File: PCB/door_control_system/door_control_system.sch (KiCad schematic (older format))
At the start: 48 parts, among them K1 DIPxx-1Axx-13x, Q1 2N7000, Q10 BSS84, Q11 BSS84, Q12 BSS84, Q13 BSS84, Q14 2N7000, Q15 2N7000, Q16 2N7000, Q17 2N7000, Q2 2N7000, Q3 2N7000, Q4 2N7000, Q5 2N7000, Q6 2N7000, Q7 2N7000, Q8 2N7000, Q9 2N7000, SW1 SW_MEC_5G, SW10 SW_MEC_5G, SW11 SW_MEC_5G, SW12 SW_MEC_5G, SW2 SW_MEC_5G, SW3 SW_MEC_5G, SW4 SW_MEC_5G, SW5 SW_MEC_5G, SW6 SW_MEC_5G, SW7 SW_MEC_5G, SW8 SW_MEC_5G, SW9 SW_MEC_5G, U1 HDSP-A401, U2 HDSP-A401, U3 HDSP-A401, U4 HDSP-A401

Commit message: Update schematic add lock controller and lock controller tb
- Schematic
- Lock controller + TB
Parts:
- added C1: 100u, symbol Device:CP
- added C2: 4u7, symbol Device:CP
- added FB1: Ferrite_Bead, symbol Device:Ferrite_Bead
- added J1, J2, J3: Conn_02x06_Top_Bottom, symbol Connector_Generic:Conn_02x06_Top_Bottom
- added J4: Barrel_Jack, symbol Connector:Barrel_Jack
- added J5: Screw_Terminal_01x02, symbol Connector:Screw_Terminal_01x02
- added R14, R15, R16, R18, R19, R20, R21, R22, R23, R24, R25, R26, R27, R28, R29, R30: 10k, symbol Device:R
- added R17: 100R, symbol Device:R
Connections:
- net labels added: FPGA_DO, VCC
- net labels removed: +5V, DOOR_SOLENOID, FPGA_DOOR_OPEN
- wire segments 225 -> 340
- no-connect marks 0 -> 4
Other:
- moved on the sheet: D1, K1, Q7, R1

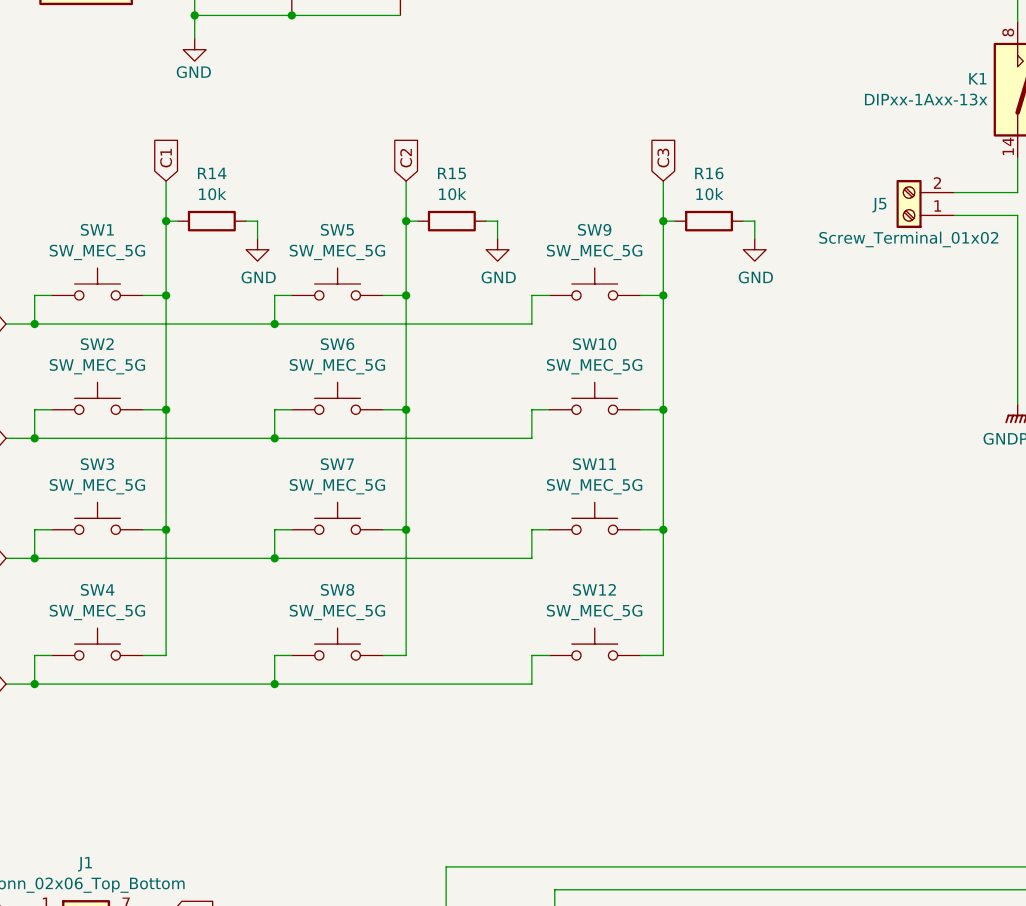
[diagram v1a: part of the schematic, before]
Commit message: Add waveform and fix schematic
Add waveform and fix schematic
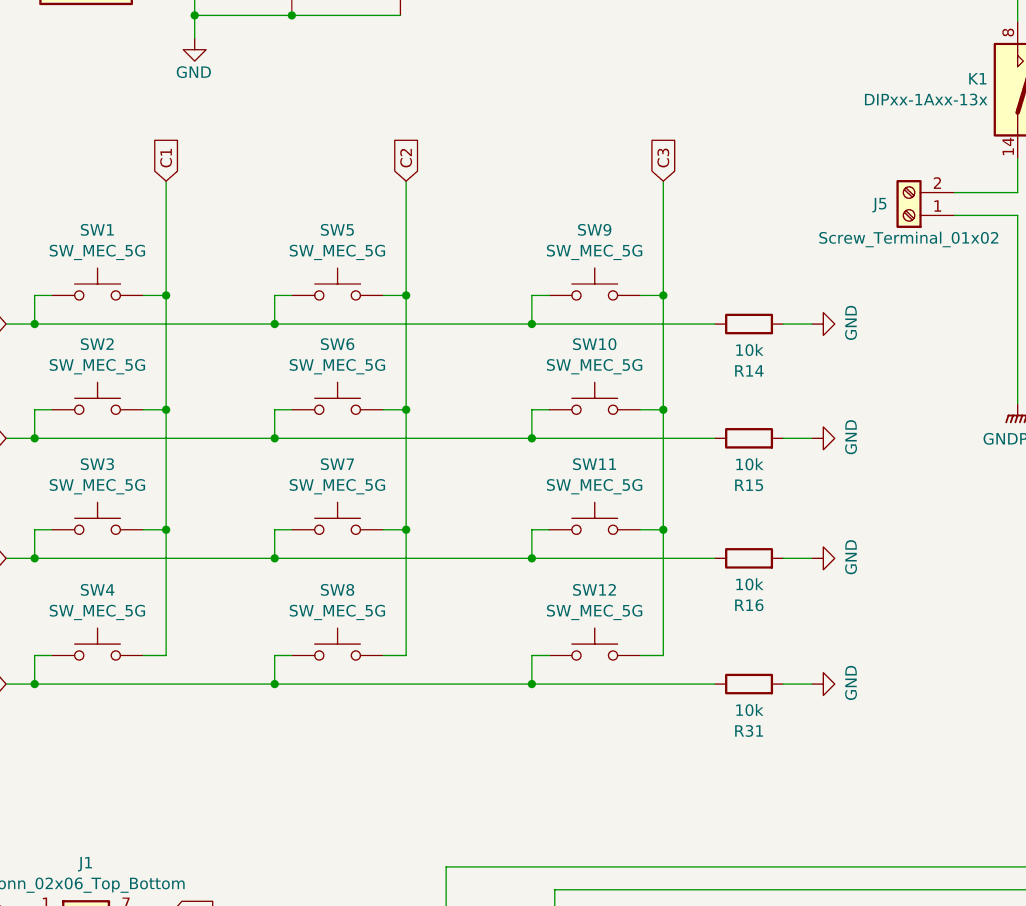
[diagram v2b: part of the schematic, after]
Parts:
- added R31: 10k, symbol Device:R
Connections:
- net C1: no longer R14.2
- net C2: no longer R15.2
- net C3: no longer R16.2
- net GND: now also R14.2, R15.2, R16.2, R31.2; no longer R14.1, R15.1, R16.1
- net R1: now also R14.1
- net R2: now also R15.1
- net R3: now also R16.1
- net R4: now also R31.1
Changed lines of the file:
@@
 	3875 2425 3975 2425
 Wire Wire Line
-	3975 2425 3975 2100
-Wire Wire Line
 	2750 2425 2850 2425
-Wire Wire Line
-	2850 2425 2850 2100
 Wire Wire Line
 	1700 2425 1800 2425
@@
 Text GLabel 3975 1925 1    50   Input ~ 0
 C3
-Text GLabel 1100 2550 0    50   Input ~ 0
-R1
-Text GLabel 1100 3050 0    50   Input ~ 0
-R2
-Text GLabel 1100 3575 0    50   Input ~ 0
-R3
-Text GLabel 1100 4125 0    50   Input ~ 0
-R4
 Wire Wire Line
 	1300 2925 1225 2925
@@
 Wire Wire Line
 	1225 4125 1100 4125
-$Comp
-L Device:R R14
-U 1 1 60801366
-P 2000 2100
-F 0 "R14" V 1793 2100 50  0000 C CNN
-F 1 "10k" V 1884 2100 50  0000 C CNN
-F 2 "" V 1930 2100 50  0001 C CNN
-F 3 "~" H 2000 2100 50  0001 C CNN
-	1    2000 2100
-	0    1    1    0
-$EndComp
-$Comp
-L my_power:GND #PWR017
-U 1 1 60832058
-P 2200 2175
-F 0 "#PWR017" H 2200 1925 50  0001 C CNN
-F 1 "GND" H 2205 2002 50  0000 C CNN
-F 2 "" H 2200 2175 50  0001 C CNN
-F 3 "" H 2200 2175 50  0001 C CNN
-	1    2200 2175
-	1    0    0    -1
-$EndComp
-Wire Wire Line
-	1800 1925 1800 2100
-Wire Wire Line
-	2200 2175 2200 2100
-Wire Wire Line
-	2200 2100 2150 2100
-Wire Wire Line
-	1850 2100 1800 2100
-Connection ~ 1800 2100
-Wire Wire Line
-	1800 2100 1800 2425
-$Comp
-L Device:R R15
-U 1 1 608D839D
-P 3050 2100
-F 0 "R15" V 2843 2100 50  0000 C CNN
-F 1 "10k" V 2934 2100 50  0000 C CNN
-F 2 "" V 2980 2100 50  0001 C CNN
-F 3 "~" H 3050 2100 50  0001 C CNN
-	1    3050 2100
-	0    1    1    0
-$EndComp
-$Comp
-L my_power:GND #PWR018
-U 1 1 608D83A3
-P 3250 2175
-F 0 "#PWR018" H 3250 1925 50  0001 C CNN
-F 1 "GND" H 3255 2002 50  0000 C CNN
-F 2 "" H 3250 2175 50  0001 C CNN
-F 3 "" H 3250 2175 50  0001 C CNN
-	1    3250 2175
-	1    0    0    -1
-$EndComp
-Wire Wire Line
-	3250 2175 3250 2100
-Wire Wire Line
-	3250 2100 3200 2100
-Wire Wire Line
-	2900 2100 2850 2100
-Connection ~ 2850 2100
-Wire Wire Line
-	2850 2100 2850 1925
-$Comp
-L Device:R R16
-U 1 1 608EA9CD
-P 4175 2100
-F 0 "R16" V 3968 2100 50  0000 C CNN
-F 1 "10k" V 4059 2100 50  0000 C CNN
-F 2 "" V 4105 2100 50  0001 C CNN
-F 3 "~" H 4175 2100 50  0001 C CNN
-	1    4175 2100
-	0    1    1    0
-$EndComp
-$Comp
-L my_power:GND #PWR019
-U 1 1 608EA9D3
-P 4375 2175
-F 0 "#PWR019" H 4375 1925 50  0001 C CNN
-F 1 "GND" H 4380 2002 50  0000 C CNN
-F 2 "" H 4375 2175 50  0001 C CNN
-F 3 "" H 4375 2175 50  0001 C CNN
-	1    4375 2175
-	1    0    0    -1
-$EndComp
-Wire Wire Line
-	4375 2175 4375 2100
-Wire Wire Line
-	4375 2100 4325 2100
-Wire Wire Line
-	4025 2100 3975 2100
-Connection ~ 3975 2100
-Wire Wire Line
-	3975 2100 3975 1925
 Wire Wire Line
 	6075 5525 6075 6300
@@
 Wire Wire Line
 	5525 1825 5525 1975
+Wire Wire Line
+	1800 1925 1800 2425
+Wire Wire Line
+	2850 1925 2850 2425
+Wire Wire Line
+	3975 1925 3975 2425
+$Comp
+L my_power:GND #PWR035
+U 1 1 608A0FBA
+P 4625 4125
+F 0 "#PWR035" H 4625 3875 50  0001 C CNN
+F 1 "GND" H 4630 3952 50  0000 C CNN
+F 2 "" H 4625 4125 50  0001 C CNN
+F 3 "" H 4625 4125 50  0001 C CNN
+	1    4625 4125
+	0    -1   -1   0
+$EndComp
+Wire Wire Line
+	4500 4125 4625 4125
+$Comp
+L Device:R R31
+U 1 1 608A0FB4
+P 4350 4125
+F 0 "R31" V 4143 4125 50  0000 C CNN
+F 1 "10k" V 4234 4125 50  0000 C CNN
+F 2 "" V 4280 4125 50  0001 C CNN
+F 3 "~" H 4350 4125 50  0001 C CNN
+	1    4350 4125
+	0    -1   -1   0
+$EndComp
+Text GLabel 1100 2550 0    50   Input ~ 0
+R1
+Text GLabel 1100 3050 0    50   Input ~ 0
+R2
+Text GLabel 1100 3575 0    50   Input ~ 0
+R3
+Text GLabel 1100 4125 0    50   Input ~ 0
+R4
+Wire Wire Line
+	4200 4125 3400 4125
+Connection ~ 3400 4125
+$Comp
+L my_power:GND #PWR019
+U 1 1 609B5E92
+P 4625 3575
+F 0 "#PWR019" H 4625 3325 50  0001 C CNN
+F 1 "GND" H 4630 3402 50  0000 C CNN
+F 2 "" H 4625 3575 50  0001 C CNN
+F 3 "" H 4625 3575 50  0001 C CNN
+	1    4625 3575
+	0    -1   -1   0
+$EndComp
+Wire Wire Line
+	4500 3575 4625 3575
+$Comp
+L Device:R R16
+U 1 1 609B5E99
+P 4350 3575
+F 0 "R16" V 4143 3575 50  0000 C CNN
+F 1 "10k" V 4234 3575 50  0000 C CNN
+F 2 "" V 4280 3575 50  0001 C CNN
+F 3 "~" H 4350 3575 50  0001 C CNN
+	1    4350 3575
+	0    -1   -1   0
+$EndComp
+Wire Wire Line
+	4200 3575 3400 3575
+Connection ~ 3400 3575
+$Comp
+L my_power:GND #PWR018
+U 1 1 60A22D19
+P 4625 3050
+F 0 "#PWR018" H 4625 2800 50  0001 C CNN
+F 1 "GND" H 4630 2877 50  0000 C CNN
+F 2 "" H 4625 3050 50  0001 C CNN
+F 3 "" H 4625 3050 50  0001 C CNN
+	1    4625 3050
+	0    -1   -1   0
+$EndComp
+Wire Wire Line
+	4500 3050 4625 3050
+$Comp
+L Device:R R15
+U 1 1 60A22D20
+P 4350 3050
+F 0 "R15" V 4143 3050 50  0000 C CNN
+F 1 "10k" V 4234 3050 50  0000 C CNN
+F 2 "" V 4280 3050 50  0001 C CNN
+F 3 "~" H 4350 3050 50  0001 C CNN
+	1    4350 3050
+	0    -1   -1   0
+$EndComp
+Wire Wire Line
+	4200 3050 3400 3050
+Connection ~ 3400 3050
+$Comp
+L my_power:GND #PWR017
+U 1 1 60A905B2
+P 4625 2550
+F 0 "#PWR017" H 4625 2300 50  0001 C CNN
+F 1 "GND" H 4630 2377 50  0000 C CNN
+F 2 "" H 4625 2550 50  0001 C CNN
+F 3 "" H 4625 2550 50  0001 C CNN
+	1    4625 2550
+	0    -1   -1   0
+$EndComp
+Wire Wire Line
+	4500 2550 4625 2550
+$Comp
+L Device:R R14
+U 1 1 60A905B9
+P 4350 2550
+F 0 "R14" V 4143 2550 50  0000 C CNN
+F 1 "10k" V 4234 2550 50  0000 C CNN
+F 2 "" V 4280 2550 50  0001 C CNN
+F 3 "~" H 4350 2550 50  0001 C CNN
+	1    4350 2550
+	0    -1   -1   0
+$EndComp
+Wire Wire Line
+	4200 2550 3400 2550
+Connection ~ 3400 2550
 $EndSCHEMATC

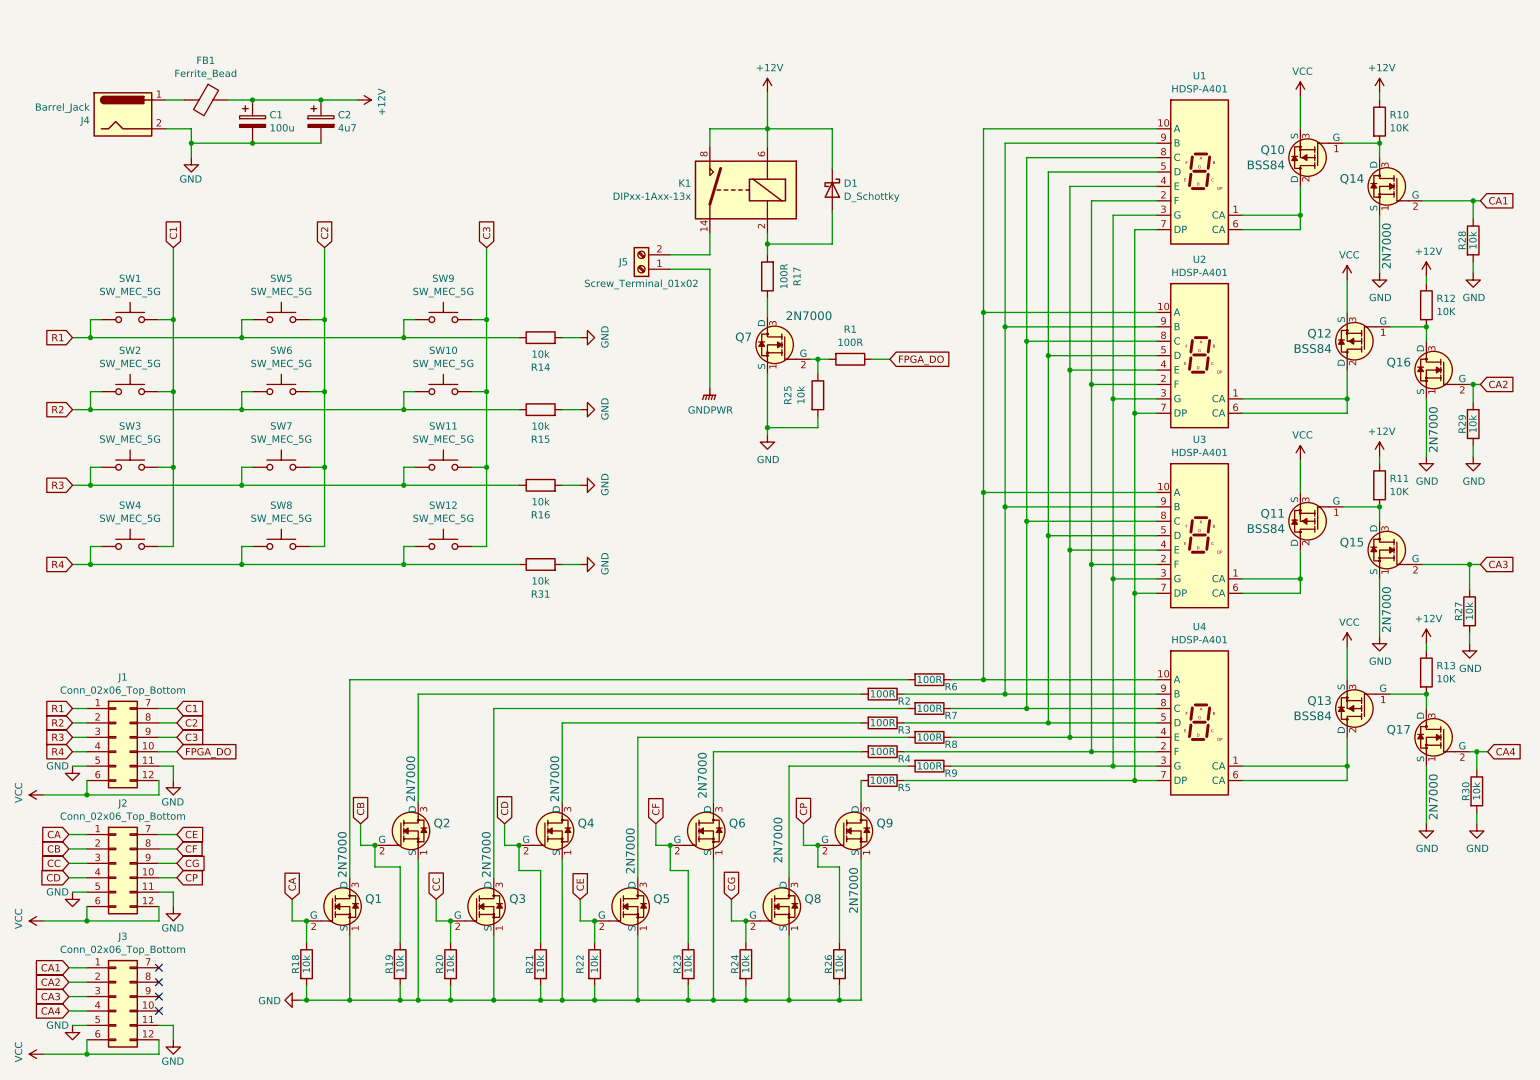
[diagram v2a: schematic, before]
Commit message: Add top and tb_top
+ minor fixes
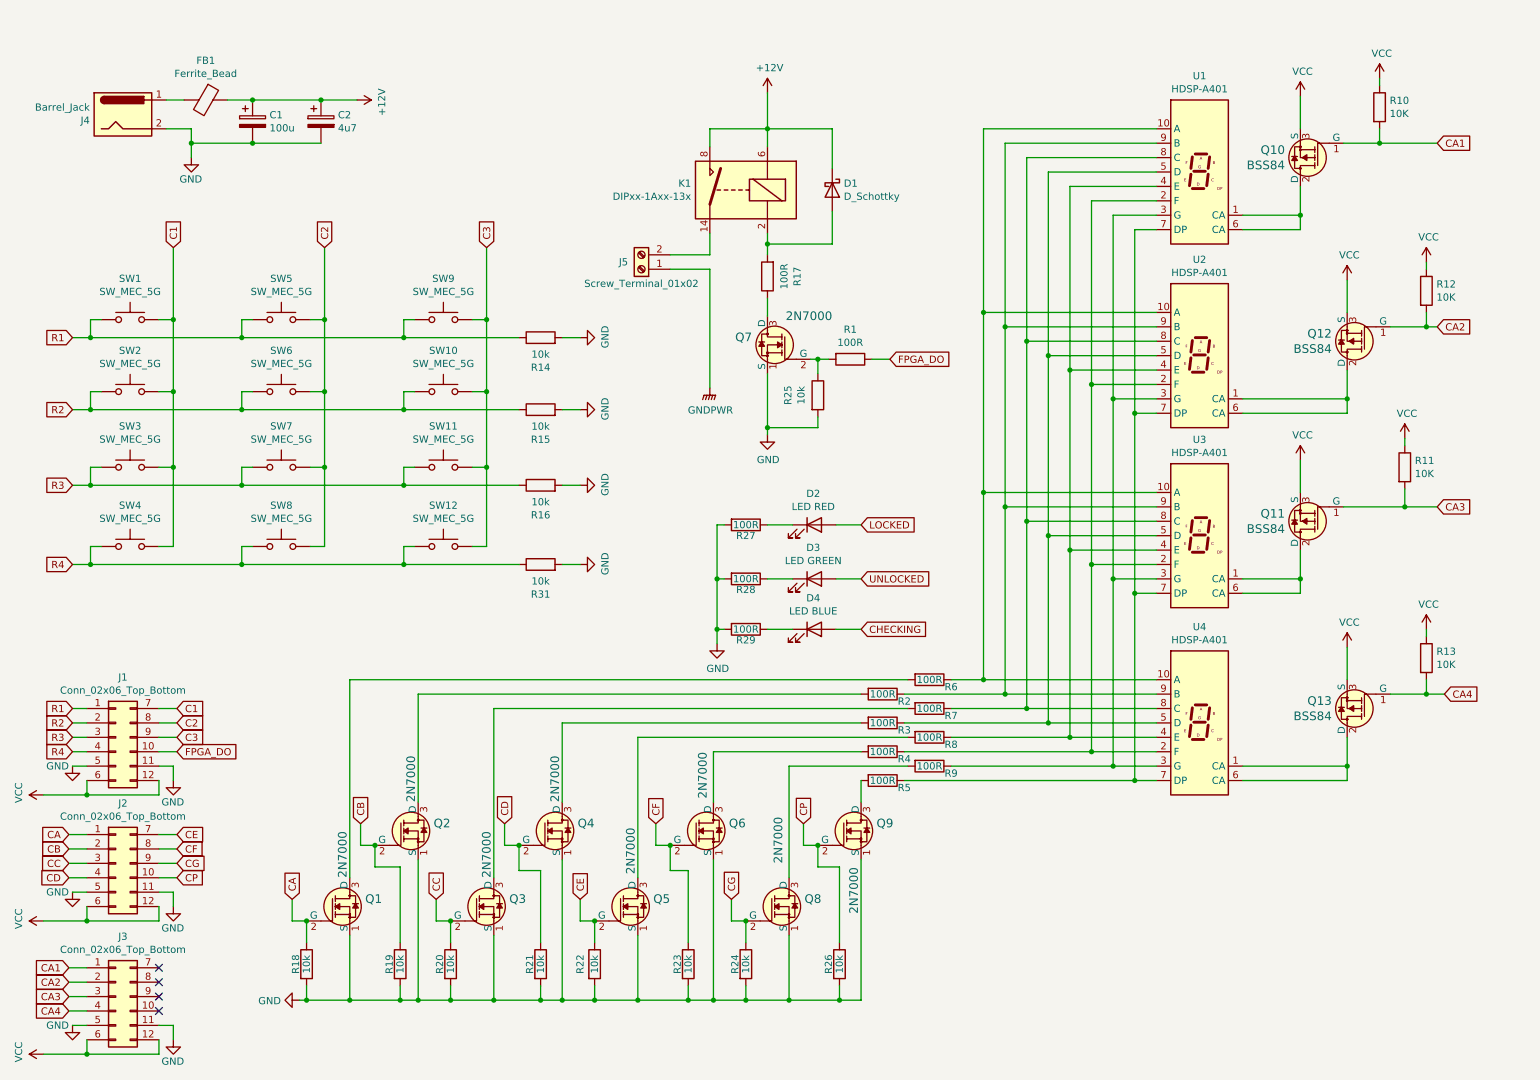
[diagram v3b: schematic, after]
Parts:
- removed Q14, Q15, Q16, Q17: 2N7000, digikey-footprints:TO-92-3, symbol dk_Transistors-FETs-MOSFETs-Single:2N7000
- removed R30: 10k, symbol Device:R
- added D2: LED RED, symbol Device:LED
- added D3: LED GREEN, symbol Device:LED
- added D4: LED BLUE, symbol Device:LED
- R27, R28, R29: value 10k -> 100R
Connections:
- net +12V: no longer R10.1, R11.1, R12.1, R13.1
- net CA1: now also Q10.1 (G), R10.2; no longer R28.1
- net CA2: now also Q12.1 (G), R12.2; no longer R29.1
- net CA3: now also Q11.1 (G), R11.2; no longer R27.1
- net CA4: now also Q13.1 (G), R13.2
- net VCC: now also R10.1, R11.1, R12.1, R13.1
- new net: D2.1 (K), R27.1
- new net: D3.1 (K), R28.1
- new net: D4.1 (K), R29.1
- new net CHECKING: D4.2 (A)
- new net LOCKED: D2.2 (A)
- new net UNLOCKED: D3.2 (A)
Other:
- moved on the sheet: R10, R11, R12, R13

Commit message: Update
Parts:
- added R30: 10k, symbol Device:R
- added SW13: SW_MEC_5G, symbol Switch:SW_MEC_5G
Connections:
- net GND: now also R30.2
- net VCC: now also SW13.3 (B), SW13.4 (B)
- new net RST: R30.1, SW13.1 (A), SW13.2 (A)
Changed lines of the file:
@@
 Text GLabel 6575 4575 2    50   Input ~ 0
 CHECKING
+$Comp
+L Switch:SW_MEC_5G SW13
+U 1 1 6088D737
+P 2875 4650
+F 0 "SW13" H 2875 4935 50  0000 C CNN
+F 1 "SW_MEC_5G" H 2875 4844 50  0000 C CNN
+F 2 "" H 2875 4850 50  0001 C CNN
+F 3 "http://www.apem.com/int/index.php?controller=attachment&id_attachment=488" H 2875 4850 50  0001 C CNN
+	1    2875 4650
+	1    0    0    -1
+$EndComp
+$Comp
+L my_power:VCC #PWR015
+U 1 1 60891AF7
+P 3275 4650
+F 0 "#PWR015" H 3275 4500 50  0001 C CNN
+F 1 "VCC" H 3290 4823 50  0000 C CNN
+F 2 "" H 3275 4650 50  0001 C CNN
+F 3 "" H 3275 4650 50  0001 C CNN
+	1    3275 4650
+	0    1    1    0
+$EndComp
+Wire Wire Line
+	3275 4650 3075 4650
+Wire Wire Line
+	2675 4650 2575 4650
+Text GLabel 2400 4650 0    50   Input ~ 0
+RST
+$Comp
+L Device:R R30
+U 1 1 608FFA4E
+P 2575 4875
+F 0 "R30" V 2368 4875 50  0000 C CNN
+F 1 "10k" V 2459 4875 50  0000 C CNN
+F 2 "" V 2505 4875 50  0001 C CNN
+F 3 "~" H 2575 4875 50  0001 C CNN
+	1    2575 4875
+	1    0    0    -1
+$EndComp
+$Comp
+L my_power:GND #PWR010
+U 1 1 60901309
+P 2575 5125
+F 0 "#PWR010" H 2575 4875 50  0001 C CNN
+F 1 "GND" H 2650 4975 50  0000 R CNN
+F 2 "" H 2575 5125 50  0001 C CNN
+F 3 "" H 2575 5125 50  0001 C CNN
+	1    2575 5125
+	1    0    0    -1
+$EndComp
+Wire Wire Line
+	2575 5125 2575 5025
+Wire Wire Line
+	2575 4725 2575 4650
+Connection ~ 2575 4650
+Wire Wire Line
+	2400 4650 2575 4650
 $EndSCHEMATC

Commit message: Update readme
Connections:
- net CHECKING: now also J3.9 (Pin_9)
- net LOCKED: now also J3.8 (Pin_8)
- net RST: now also J3.10 (Pin_10)
- net UNLOCKED: now also J3.7 (Pin_7)
- no-connect marks 4 -> 0
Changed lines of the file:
@@
 Text GLabel 1075 7225 0    50   Input ~ 0
 CA4
-NoConn ~ 1700 6925
-NoConn ~ 1700 7025
-NoConn ~ 1700 7125
-NoConn ~ 1700 7225
 $Comp
 L Device:R R25
@@
 Wire Wire Line
 	2400 4650 2575 4650
+Text GLabel 1825 7225 2    50   Input ~ 0
+RST
+Text GLabel 1825 7025 2    50   Input ~ 0
+LOCKED
+Text GLabel 1825 6925 2    50   Input ~ 0
+UNLOCKED
+Text GLabel 1825 7125 2    50   Input ~ 0
+CHECKING
+Wire Wire Line
+	1700 7225 1825 7225
+Wire Wire Line
+	1700 7125 1825 7125
+Wire Wire Line
+	1700 7025 1825 7025
+Wire Wire Line
+	1700 6925 1825 6925
 $EndSCHEMATC

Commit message: add top to rm, fix some stuff, etc.
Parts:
- added J6: Screw_Terminal_01x01, symbol Connector:Screw_Terminal_01x01
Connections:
- net GNDPWR: now also J6.1 (Pin_1)
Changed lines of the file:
@@
 L my_power:GNDPWR #PWR02
 U 1 1 606E8472
-P 5525 2900
-F 0 "#PWR02" H 5525 2700 50  0001 C CNN
-F 1 "GNDPWR" H 5529 2746 50  0000 C CNN
-F 2 "" H 5525 2850 50  0001 C CNN
-F 3 "" H 5525 2850 50  0001 C CNN
-	1    5525 2900
+P 5100 2775
+F 0 "#PWR02" H 5100 2575 50  0001 C CNN
+F 1 "GNDPWR" H 5100 2625 50  0000 C CNN
+F 2 "" H 5100 2725 50  0001 C CNN
+F 3 "" H 5100 2725 50  0001 C CNN
+	1    5100 2775
 	1    0    0    -1
 $EndComp
@@
 $EndComp
 Wire Wire Line
-	5250 2075 5525 2075
-Wire Wire Line
-	5525 2075 5525 2900
-Wire Wire Line
 	5525 1975 5250 1975
 Wire Wire Line
@@
 Wire Wire Line
 	1700 6925 1825 6925
+$Comp
+L Connector:Screw_Terminal_01x01 J6
+U 1 1 608D9259
+P 5525 2950
+F 0 "J6" V 5397 3030 50  0000 L CNN
+F 1 "Screw_Terminal_01x01" V 5650 2375 50  0000 L CNN
+F 2 "" H 5525 2950 50  0001 C CNN
+F 3 "~" H 5525 2950 50  0001 C CNN
+	1    5525 2950
+	0    1    1    0
+$EndComp
+Wire Wire Line
+	5525 2550 5525 2750
+Wire Wire Line
+	5100 2775 5100 2550
+Wire Wire Line
+	5100 2550 5525 2550
+Wire Wire Line
+	5250 2075 5525 2075
+Wire Wire Line
+	5525 2550 5525 2075
+Connection ~ 5525 2550
 $EndSCHEMATC
